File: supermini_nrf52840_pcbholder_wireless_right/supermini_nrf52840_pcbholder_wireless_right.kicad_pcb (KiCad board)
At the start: 2 copper layers, 39.9 x 38.4 mm, 11 parts, among them J1 Conn_01x02, J2 Conn_01x04, J3 Conn_01x07, J4 Conn_01x07, SW1 SW_SPDT, SW2 SW_SPST, U1 nice_nano

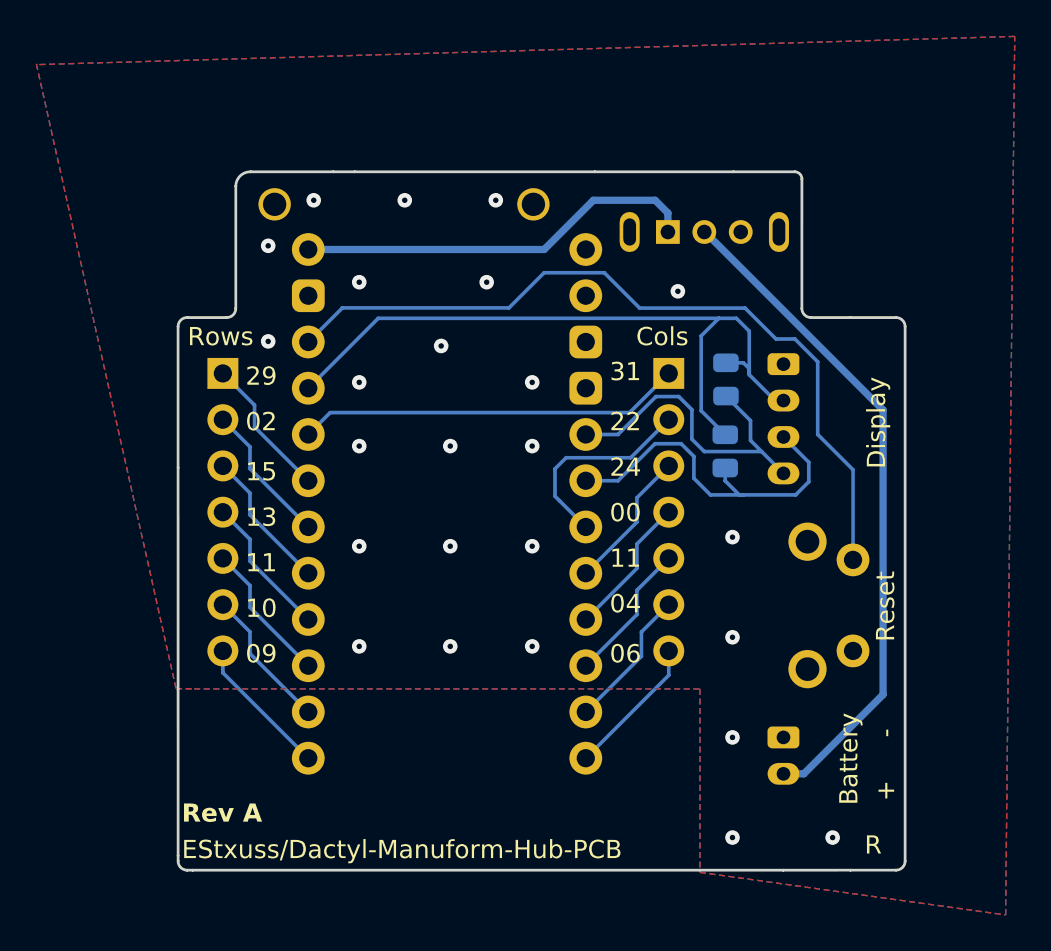
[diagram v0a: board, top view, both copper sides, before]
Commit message: edge cuts change
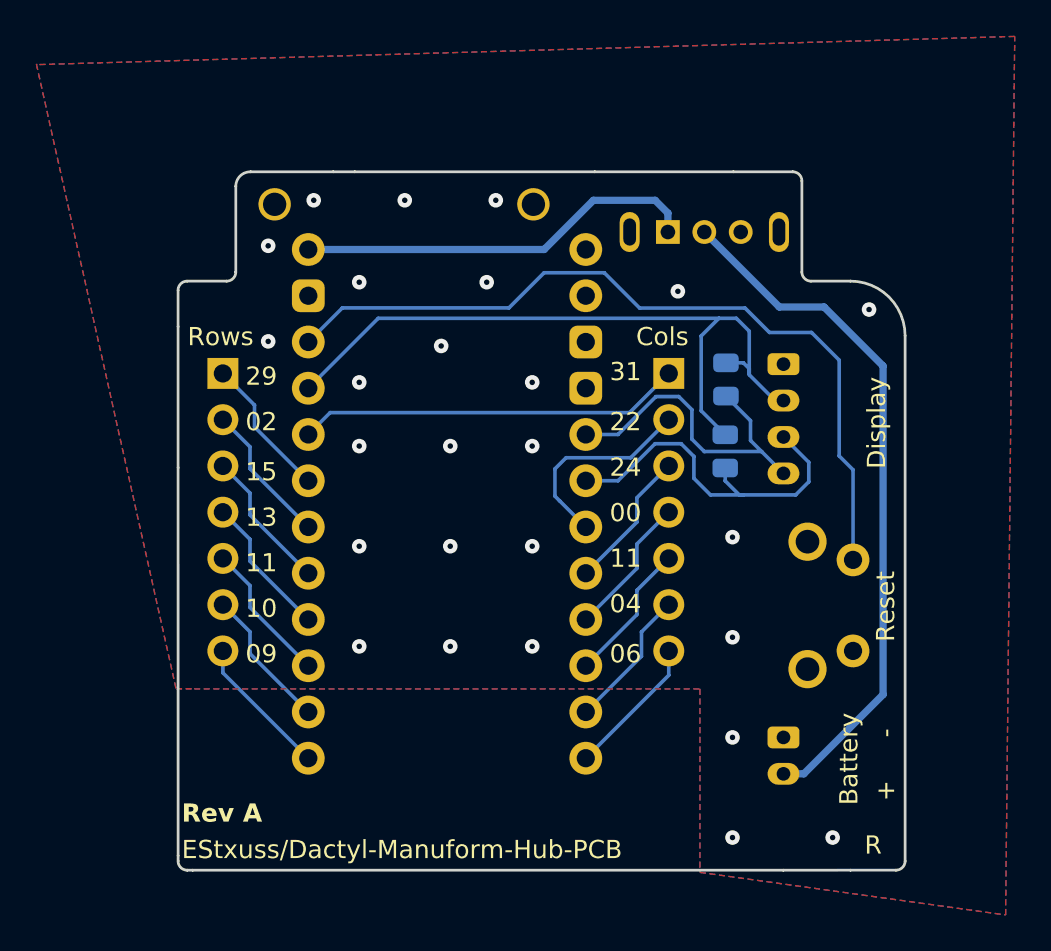
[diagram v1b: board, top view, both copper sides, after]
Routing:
- net /BATT_SW_POS: track 36.8 -> 38.2 mm
- net Net-(SW2-A): track 43.3 -> 44.0 mm
- net GND: vias 25 -> 26
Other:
- outline, holes or cut-outs redrawn
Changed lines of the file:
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@@
 		)
+	)
+	(gr_arc
+		(start 152.98 67.94)
+		(mid 155.10132 68.81868)
+		(end 155.98 70.94)
+		(stroke
+			(width 0.15)
+			(type default)
+		)
+		(layer "Edge.Cuts")
+	)
+	(gr_arc
+		(start 150.81025 67.94)
+		(mid 150.456609 67.793465)
+		(end 150.31025 67.439751)
+		(stroke
+			(width 0.15)
+			(type default)
+		)
+		(layer "Edge.Cuts")
 	)
 	(gr_line
@@
 	)
 	(gr_arc
-		(start 119.220156 69.440156)
-		(mid 119.073652 69.793593)
-		(end 118.720156 69.94)
+		(start 116.049987 68.440009)
+		(mid 116.19643 68.08645)
+		(end 116.549987 67.94)
 		(stroke
 			(width 0.15)
@@
 	(gr_line
 		(start 155.98 99.790049)
-		(end 155.98 70.44)
+		(end 155.98 70.94)
 		(stroke
 			(width 0.15)
@@
 	)
 	(gr_line
+		(start 116.549987 67.94)
+		(end 118.720216 67.94)
+		(stroke
+			(width 0.15)
+			(type default)
+		)
+		(layer "Edge.Cuts")
+	)
+	(gr_line
 		(start 116.052176 99.492483)
 		(end 116.051364 99.790185)
@@
 	)
 	(gr_line
-		(start 116.550022 69.94)
-		(end 118.720156 69.94)
-		(stroke
-			(width 0.15)
-			(type default)
-		)
-		(layer "Edge.Cuts")
-	)
-	(gr_line
 		(start 125.758349 61.936233)
 		(end 124.567721 61.936233)
@@
 	)
 	(gr_line
-		(start 150.312877 62.333109)
-		(end 150.310189 69.439811)
+		(start 150.310023 62.43621)
+		(end 150.31025 67.439751)
 		(stroke
 			(width 0.15)
 			(type solid)
+		)
+		(layer "Edge.Cuts")
+	)
+	(gr_line
+		(start 116.050022 70.440022)
+		(end 116.049987 68.440009)
+		(stroke
+			(width 0.15)
+			(type default)
 		)
 		(layer "Edge.Cuts")
@@
 			(width 0.15)
 			(type solid)
-		)
-		(layer "Edge.Cuts")
-	)
-	(gr_arc
-		(start 155.48 69.94)
-		(mid 155.833553 70.086447)
-		(end 155.98 70.44)
-		(stroke
-			(width 0.15)
-			(type default)
 		)
 		(layer "Edge.Cuts")
@@
 	)
 	(gr_line
-		(start 150.810189 69.94)
-		(end 152.98 69.94)
-		(stroke
-			(width 0.15)
-			(type default)
-		)
-		(layer "Edge.Cuts")
-	)
-	(gr_line
 		(start 116.052176 99.492483)
 		(end 116.05036 78.192483)
@@
 	)
 	(gr_line
-		(start 152.98 69.94)
-		(end 155.48 69.94)
-		(stroke
-			(width 0.15)
-			(type default)
-		)
-		(layer "Edge.Cuts")
-	)
-	(gr_line
-		(start 149.916001 61.936233)
+		(start 149.810023 61.936233)
 		(end 146.553481 61.936233)
 		(stroke
@@
 	)
 	(gr_arc
-		(start 150.810189 69.94)
-		(mid 150.456576 69.793483)
-		(end 150.310189 69.439811)
+		(start 149.810023 61.936233)
+		(mid 150.163568 62.082671)
+		(end 150.310023 62.43621)
+		(stroke
+			(width 0.15)
+			(type default)
+		)
+		(layer "Edge.Cuts")
+	)
+	(gr_arc
+		(start 119.220216 67.440216)
+		(mid 119.073693 67.79363)
+		(end 118.720216 67.94)
 		(stroke
 			(width 0.15)
@@
 		(layer "Edge.Cuts")
 	)
-	(gr_arc
-		(start 116.050022 70.440022)
-		(mid 116.196462 70.086462)
-		(end 116.550022 69.94)
-		(stroke
-			(width 0.15)
-			(type default)
-		)
-		(layer "Edge.Cuts")
-	)
-	(gr_arc
-		(start 149.916001 61.936233)
-		(mid 150.196656 62.052454)
-		(end 150.312877 62.333109)
-		(stroke
-			(width 0.15)
-			(type solid)
-		)
-		(layer "Edge.Cuts")
-	)
 	(gr_line
 		(start 119.222251 62.729983)
-		(end 119.220156 69.440156)
+		(end 119.220216 67.440216)
+		(stroke
+			(width 0.15)
+			(type default)
+		)
+		(layer "Edge.Cuts")
+	)
+	(gr_line
+		(start 152.98 67.94)
+		(end 150.81025 67.94)
 		(stroke
 			(width 0.15)
@@
 	)
 	(via
+		(at 154 69.5)
+		(size 0.8)
+		(drill 0.3)
+		(layers "F.Cu" "B.Cu")
+		(free yes)
+		(net 1)
+	)
+	(via
 		(at 123.5 63.5)
 		(size 0.8)
@@
 	)
 	(segment
+		(start 136.151371 67.48)
+		(end 139.46 67.48)
+		(width 0.2)
+		(layer "B.Cu")
+		(net 21)
+	)
+	(segment
+		(start 148.53 70.76)
+		(end 150.84 70.76)
+		(width 0.2)
+		(layer "B.Cu")
+		(net 21)
+	)
+	(segment
+		(start 150.84 70.76)
+		(end 152.36 72.28)
+		(width 0.2)
+		(layer "B.Cu")
+		(net 21)
+	)
+	(segment
+		(start 147.19 69.42)
+		(end 148.53 70.76)
+		(width 0.2)
+		(layer "B.Cu")
+		(net 21)
+	)
+	(segment
 		(start 153.12 78.3)
 		(end 153.12 83.25)
@@
 	)
 	(segment
+		(start 152.36 77.54)
+		(end 153.12 78.3)
+		(width 0.2)
+		(layer "B.Cu")
+		(net 21)
+	)
+	(segment
+		(start 134.221371 69.41)
+		(end 136.151371 67.48)
+		(width 0.2)
+		(layer "B.Cu")
+		(net 21)
+	)
+	(segment
+		(start 153.12 83.25)
+		(end 153.11 83.24)
+		(width 0.2)
+		(layer "B.Cu")
+		(net 21)
+	)
+	(segment
+		(start 123.202176 71.282483)
+		(end 125.074659 69.41)
+		(width 0.2)
+		(layer "B.Cu")
+		(net 21)
+	)
+	(segment
+		(start 139.46 67.48)
+		(end 141.4 69.42)
+		(width 0.2)
+		(layer "B.Cu")
+		(net 21)
+	)
+	(segment
 		(start 141.4 69.42)
 		(end 147.19 69.42)
@@
 	)
 	(segment
-		(start 149.93 71.12)
-		(end 151.18 72.37)
+		(start 152.36 72.28)
+		(end 152.36 77.54)
 		(width 0.2)
 		(layer "B.Cu")
@@
 	)
 	(segment
-		(start 139.46 67.48)
-		(end 141.4 69.42)
-		(width 0.2)
-		(layer "B.Cu")
-		(net 21)
-	)
-	(segment
-		(start 151.18 72.37)
-		(end 151.18 76.36)
-		(width 0.2)
-		(layer "B.Cu")
-		(net 21)
-	)
-	(segment
-		(start 148.89 71.12)
-		(end 149.93 71.12)
-		(width 0.2)
-		(layer "B.Cu")
-		(net 21)
-	)
-	(segment
-		(start 136.151371 67.48)
-		(end 139.46 67.48)
-		(width 0.2)
-		(layer "B.Cu")
-		(net 21)
-	)
-	(segment
-		(start 153.12 83.25)
-		(end 153.11 83.24)
-		(width 0.2)
-		(layer "B.Cu")
-		(net 21)
-	)
-	(segment
-		(start 151.18 76.36)
-		(end 153.12 78.3)
-		(width 0.2)
-		(layer "B.Cu")
-		(net 21)
-	)
-	(segment
-		(start 147.19 69.42)
-		(end 148.89 71.12)
-		(width 0.2)
-		(layer "B.Cu")
-		(net 21)
-	)
-	(segment
-		(start 134.221371 69.41)
-		(end 136.151371 67.48)
-		(width 0.2)
-		(layer "B.Cu")
-		(net 21)
-	)
-	(segment
-		(start 123.202176 71.282483)
-		(end 125.074659 69.41)
-		(width 0.2)
-		(layer "B.Cu")
-		(net 21)
-	)
-	(segment
 		(start 154.77 90.65)
-		(end 154.77 75.02)
+		(end 154.77 72.6)
 		(width 0.4)
 		(layer "B.Cu")
@@
 	)
 	(segment
+		(start 149.069693 69.36)
+		(end 144.952176 65.242483)
+		(width 0.4)
+		(layer "B.Cu")
+		(net 24)
+	)
+	(segment
+		(start 151.53 69.36)
+		(end 149.069693 69.36)
+		(width 0.4)
+		(layer "B.Cu")
+		(net 24)
+	)
+	(segment
 		(start 149.3 95)
 		(end 150.42 95)
@@
 	)
 	(segment
-		(start 154.77 75.02)
-		(end 144.992483 65.242483)
+		(start 154.77 72.6)
+		(end 151.53 69.36)
 		(width 0.4)
 		(layer "B.Cu")
-		(net 24)
-	)
-	(segment
-		(start 144.992483 65.242483)
-		(end 144.952176 65.242483)
-		(width 0.4)
-		(layer "B.Cu")

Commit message: create left side and tweaks
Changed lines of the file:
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@@
 			(at 0 -1.65 90)
 			(layer "B.Fab")
+			(hide yes)
 			(effects
 				(font
@@
 		(sheetname "Root")
 		(sheetfile "supermini_nrf52840_pcbholder_wireless_right.kicad_sch")
-		(attr smd)
+		(attr smd dnp)
 		(fp_line
 			(start 0.227064 0.735)
@@
 		)
 		(property "Value" "Conn_01x07"
-			(at 0 -17.57 360)
+			(at 0 -17.57 0)
 			(layer "B.Fab")
 			(effects
@@
 		)
 		(property "Footprint" "Connector_PinHeader_2.54mm:PinHeader_1x07_P2.54mm_Vertical"
-			(at 0 0 360)
+			(at 0 0 0)
 			(layer "B.Fab")
 			(hide yes)
@@
 		)
 		(property "Datasheet" ""
-			(at 0 0 360)
+			(at 0 0 0)
 			(layer "B.Fab")
 			(hide yes)
@@
 		)
 		(property "Description" "Generic connector, single row, 01x07, script generated (kicad-library-utils/schlib/autogen/connector/)"
-			(at 0 0 360)
+			(at 0 0 0)
 			(layer "B.Fab")
 			(hide yes)
@@
 		(tags "alps tht dip pushbutton SPST")
 		(property "Reference" "SW2"
-			(at 0 -1.87 270)
+			(at 0 -1.87 -90)
 			(unlocked yes)
 			(layer "B.SilkS")
@@
 			(at 0 -1.65 90)
 			(layer "B.Fab")
+			(hide yes)
 			(effects
 				(font
@@
 		(sheetname "Root")
 		(sheetfile "supermini_nrf52840_pcbholder_wireless_right.kicad_sch")
-		(attr smd)
+		(attr smd dnp)
 		(fp_line
 			(start 0.227064 0.735)
@@
 	)
 	(via
-		(at 121 66)
+		(at 120.75 66)
 		(size 0.8)
 		(drill 0.3)
@@
 	)
 	(via
-		(at 121 71.25)
+		(at 120.75 71.25)
 		(size 0.8)
 		(drill 0.3)

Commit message: remove unused pins from supermini symbol
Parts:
- U1: value nice_nano -> SuperMini nRF52840
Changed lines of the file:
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@@
 			)
 		)
-		(property "Value" "nice_nano"
+		(property "Value" "SuperMini nRF52840"
 			(at 0 -0.635 0)
 			(unlocked yes)
@@
 			)
 		)
-		(property "Datasheet" "https://nicekeyboards.com/docs/nice-nano/pinout-schematic"
+		(property "Datasheet" "https://wiki.icbbuy.com/doku.php?id=developmentboard:nrf52840"
 			(at 0 0 0)
 			(unlocked yes)
@@
 			)
 		)
-		(property "Description" "Symbol for an nicekeyboards nice!nano"
+		(property "Description" "Symbol for Supermini nRF52840 with only pro micro compatible pins"
 			(at 0 0 0)
 			(unlocked yes)
@@
 			(net 21 "Net-(SW2-A)")
 			(pinfunction "RST")
-			(pintype "input")
+			(pintype "bidirectional")
 		)
 		(pad "16" thru_hole circle
